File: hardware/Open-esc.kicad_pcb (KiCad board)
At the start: 2 copper layers, 63 x 19 mm, 34 parts, among them J1 AVR-ISP-6, Q1 AO3401A, Q2 IRLML0030, Q3 AO3401A, Q4 IRLML0030, Q5 AO3401A, Q6 IRLML0030, U1 ATmega88PA-A, U2 AMS1117-3.3

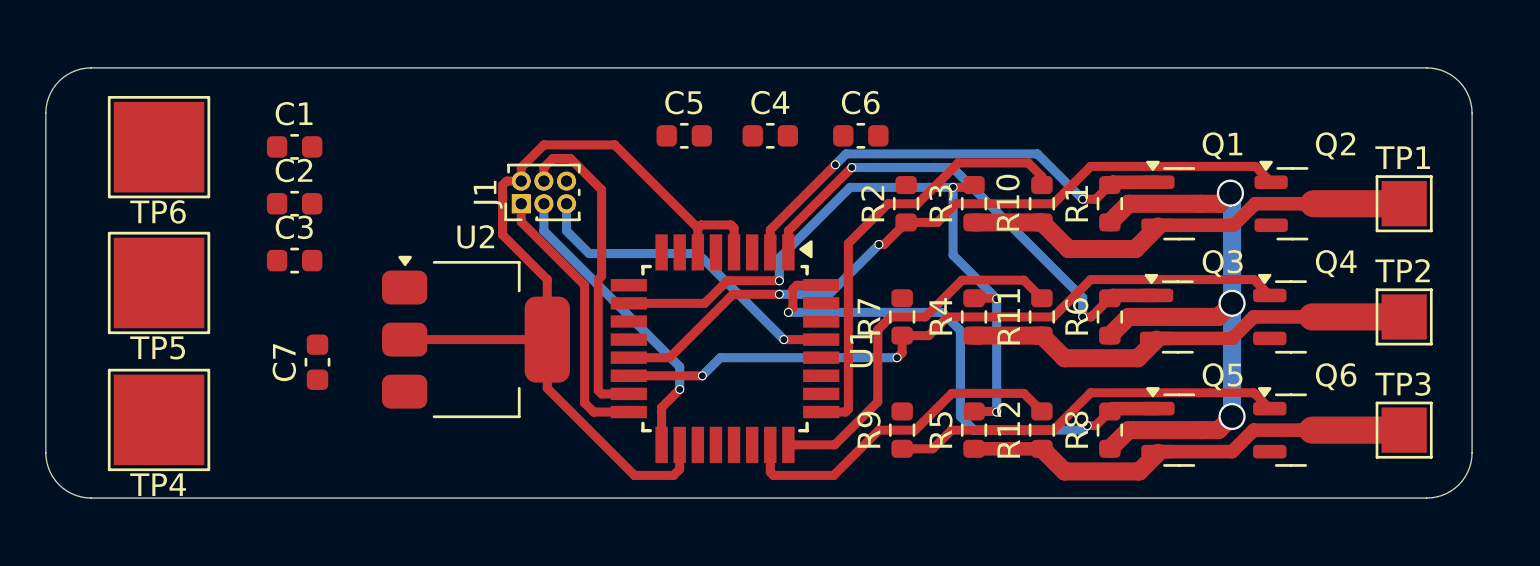
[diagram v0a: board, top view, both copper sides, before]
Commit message: rename connection and add pad wiring
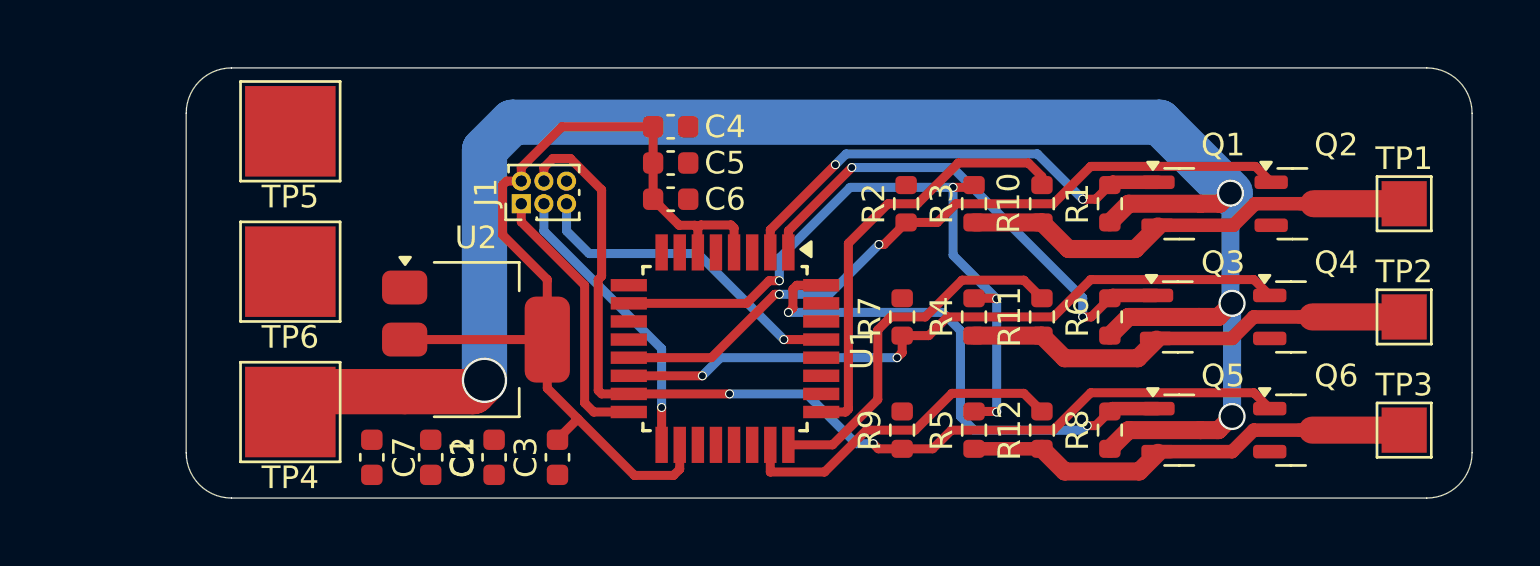
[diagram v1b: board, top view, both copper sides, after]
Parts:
- moved C1 16.3 mm to (73.8, 61.2), turned to 90 degrees
- moved C3 14.5 mm to (76.6, 61.2), turned to -90 degrees
- moved C2 12.7 mm to (71.0, 61.2), turned to -90 degrees
- moved TP5 8.86 mm to (64.8, 46.8)
- moved C6 8.85 mm to (81.6, 49.8)
- moved TP6 7.99 mm to (64.8, 53.0)
- moved TP4 5.81 mm to (64.8, 59.2)
- moved C7 4.84 mm to (68.4, 61.2), turned to -90 degrees
- moved C4 4.42 mm to (81.6, 46.6)
- moved C5 1.34 mm to (81.6, 48.2)
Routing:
- net +BATT: track 27.7 -> 81.9 mm, vias 3 -> 4
- net CL1: track 31.8 -> 44.9 mm, vias 0 -> 2
- net +5V: track 39.8 -> 43.7 mm
- net SCK1: track 13.5 -> 12.8 mm
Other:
- board size 63 x 19 mm -> 56.8 x 19 mm

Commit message: add general gnd
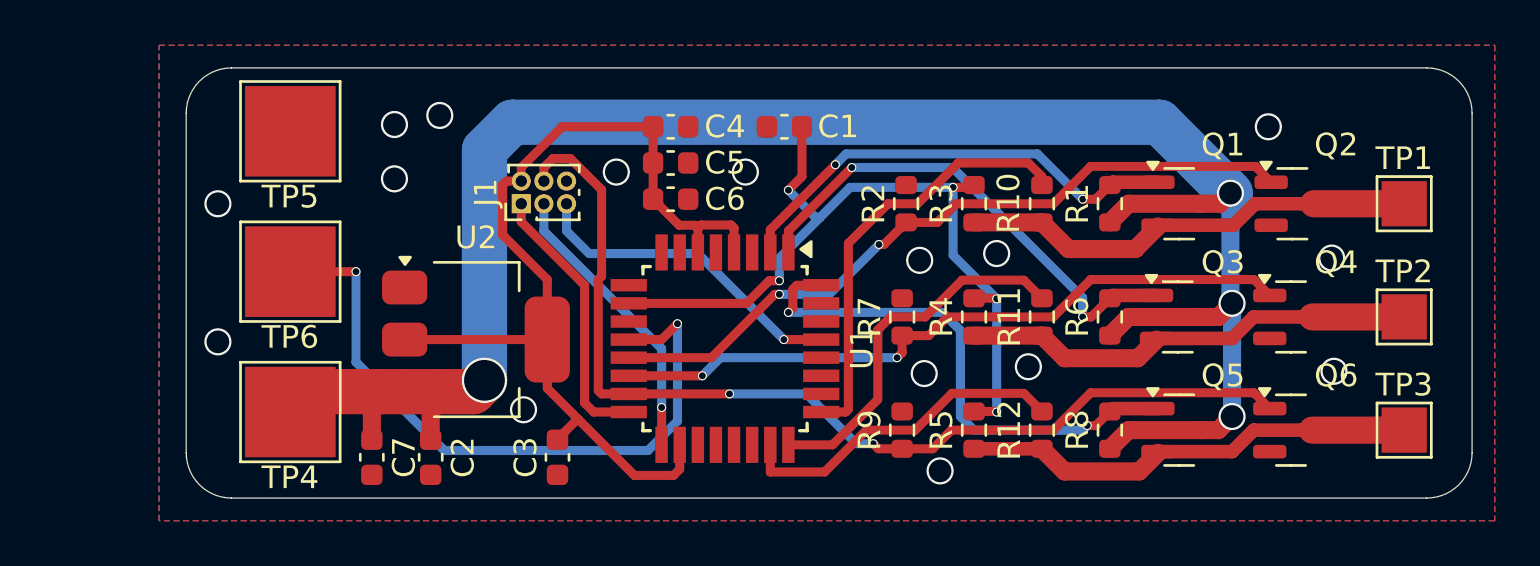
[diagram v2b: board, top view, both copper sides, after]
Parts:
- moved C1 19.4 mm to (86.6, 46.6), turned to 0 degrees
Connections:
- net A0_1 renamed A0
- net A1_1 renamed A1
- net A2_1 renamed A2
- net AH1 renamed AH
- net AL1 renamed AL
- net BH1 renamed BH
- net BL1 renamed BL
- net CH1 renamed CH
- net CL1 renamed CL
- net D6_1 renamed D6
- net PWM1 renamed PWM
- net RST1 renamed RST
- net SCK1 renamed SCK
- U1 pad 16: MISO1 -> MISO
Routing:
- net PWM: track 0.00 -> 30.0 mm, vias 0 -> 2
- net D6: track 30.7 -> 35.7 mm, vias 4 -> 5
- net +BATT: track 81.9 -> 86.5 mm
- net GND: vias 0 -> 16
- added copper zone on B.Cu, net GND
- added copper zone on F.Cu, net GND
